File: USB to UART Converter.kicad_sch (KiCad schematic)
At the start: 19 parts, among them J1 USB_C_Receptacle_USB2.0_16P, J2 Conn_01x05_Pin, U1 CP2102N-Axx-xQFN28

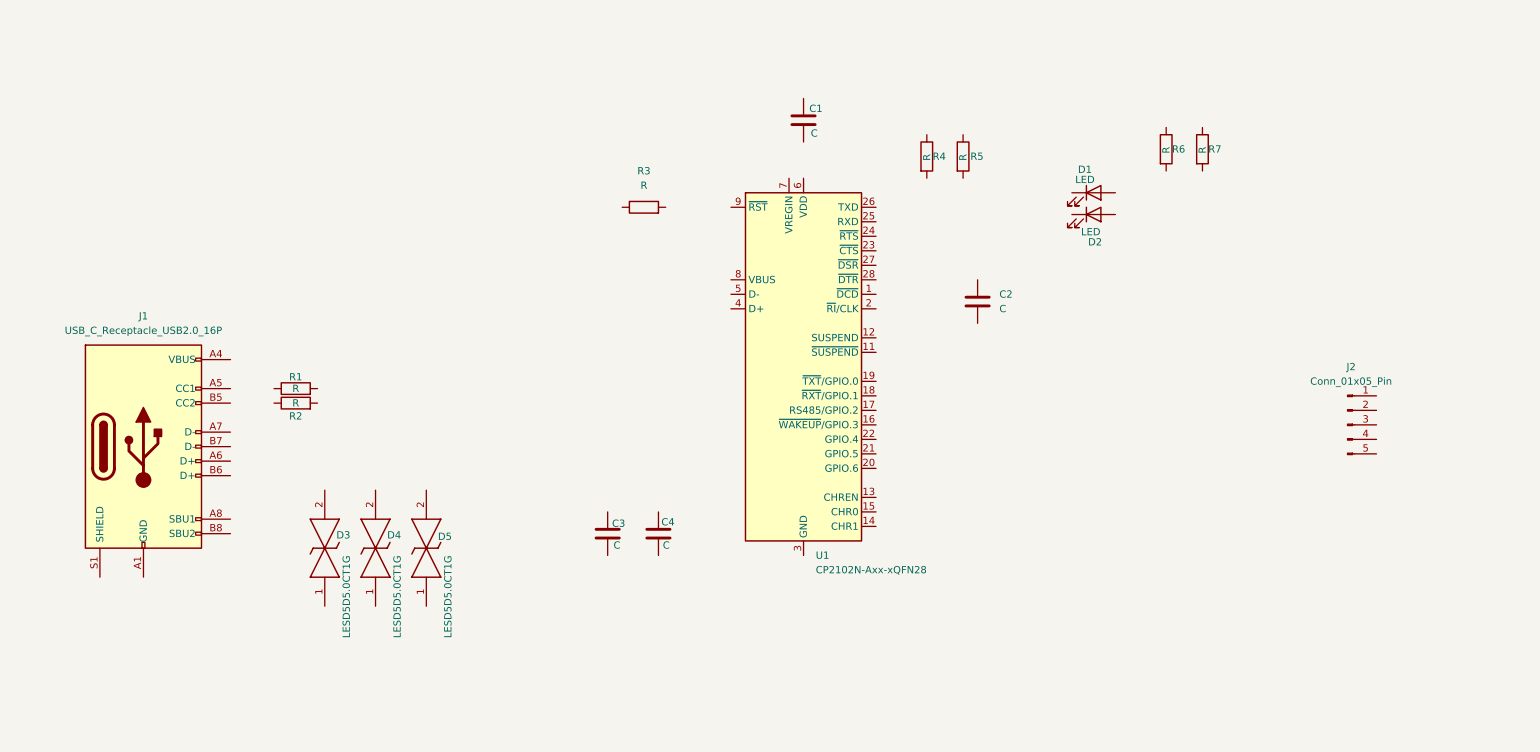
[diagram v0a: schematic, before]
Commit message: Connected with Wires in Schematic
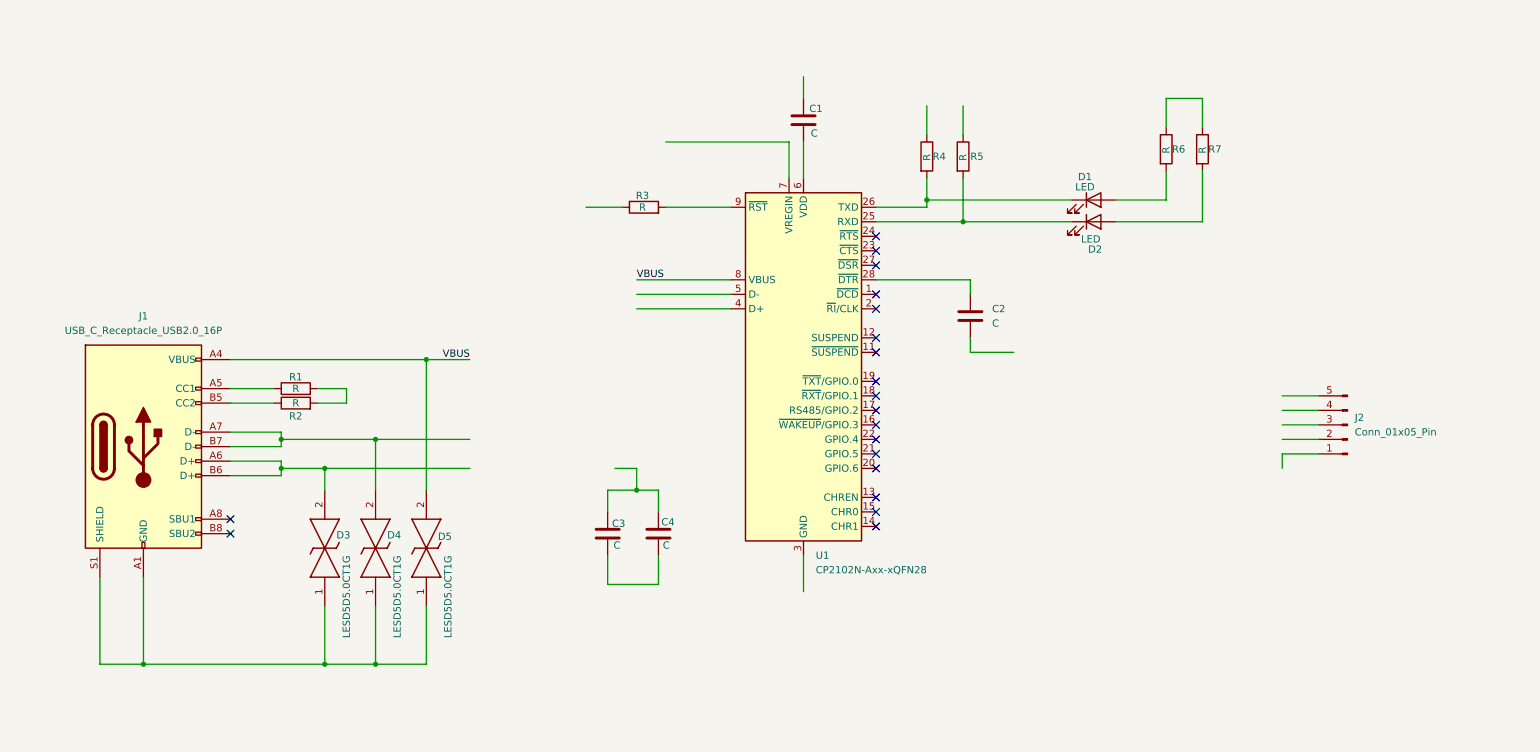
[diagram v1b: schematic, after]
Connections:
- net at D1.1 (K): now also R4.2, U1.26 (TXD)
- net at D1.2 (A): now also R6.2
- net at C1.2: now also U1.6 (VDD)
- net at R2.1: now also J1.B5 (CC2)
- net at R2.2: now also R1.2
- net at D2.1 (K): now also R5.2, U1.25 (RXD)
- net at D2.2 (A): now also R7.2
- net at U1.28 (~{DTR}): now also C2.1
- net VBUS: now reaches U1.8 (VBUS)
- net VBUS: now also D5.2, J1.A4 (VBUS), J1.A9 (VBUS), J1.B4 (VBUS), J1.B9 (VBUS)
- net at U1.9 (~{RST}): now also R3.2
- net at D4.1: now also D3.1, D5.1, J1.A1 (GND), J1.A12 (GND), J1.B1 (GND), J1.B12 (GND), J1.S1 (SHIELD)
- net at D4.2: now also J1.A7 (D-), J1.B7 (D-)
- net at R6.1: now also R7.1
- net at C4.1: now also C3.1
- net at C4.2: now also C3.2
- net at J1.A5 (CC1): now also R1.1
- net at J1.A6 (D+): now also D3.2, J1.B6 (D+)
- no-connect marks 0 -> 19
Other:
- moved on the sheet: C2, D1, D2, J2

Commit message: Added Net Labels
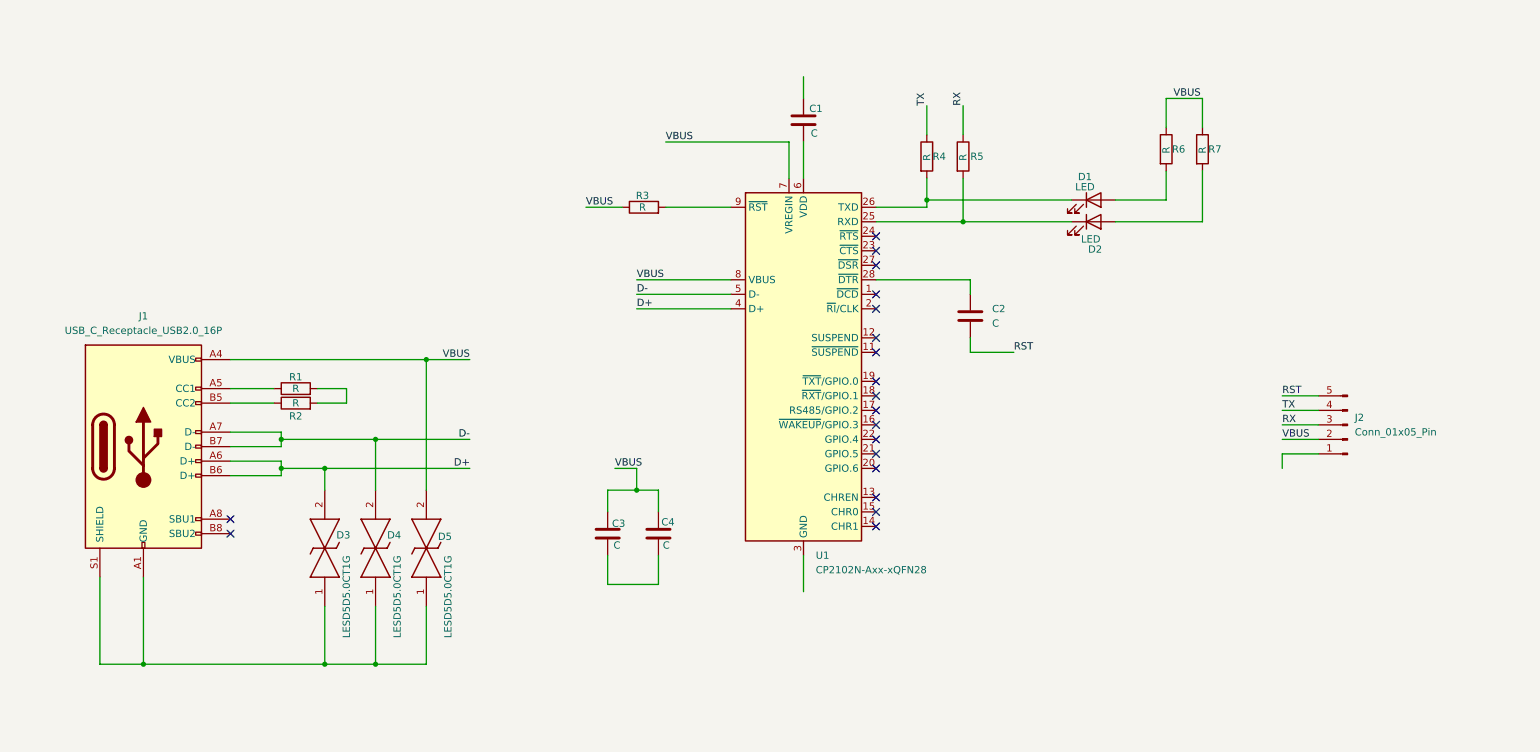
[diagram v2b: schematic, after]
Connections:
- net VBUS: now also C3.1, C4.1, J2.2 (Pin_2), R3.1, R6.1, R7.1, U1.7 (VREGIN)
- net D+: now reaches U1.4 (D+)
- net D+: now also D3.2, J1.A6 (D+), J1.B6 (D+)
- net D-: now reaches U1.5 (D-)
- net D-: now also D4.2, J1.A7 (D-), J1.B7 (D-)
- net RST: now reaches C2.2
- net RST: now also J2.5 (Pin_5)
- net RX: now reaches R5.1
- net RX: now also J2.3 (Pin_3)
- net TX: now reaches R4.1
- net TX: now also J2.4 (Pin_4)
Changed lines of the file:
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@@
+		)
+	)
+	(label "D+"
+		(at 128.27 71.12 0)
+		(effects
+			(font
+				(size 1.27 1.27)
+			)
+			(justify left bottom)
 		)
 	)
@@
 	)
 	(label "VBUS"
+		(at 133.35 41.91 0)
+		(effects
+			(font
+				(size 1.27 1.27)
+			)
+			(justify left bottom)
+		)
+	)
+	(label "D-"
+		(at 99.06 93.98 180)
+		(effects
+			(font
+				(size 1.27 1.27)
+			)
+			(justify right bottom)
+		)
+	)
+	(label "VBUS"
 		(at 128.27 66.04 0)
 		(effects
 			(font
+				(size 1.27 1.27)
+			)
+			(justify left bottom)
+		)
+	)
+	(label "VBUS"
+		(at 241.3 93.98 0)
+		(effects
+			(font
+				(size 1.27 1.27)
+			)
+			(justify left bottom)
+		)
+	)
+	(label "VBUS"
+		(at 124.46 99.06 0)
+		(effects
+			(font
+				(size 1.27 1.27)
+			)
+			(justify left bottom)
+		)
+	)
+	(label "TX"
+		(at 179.07 35.56 90)
+		(effects
+			(font
+				(size 1.27 1.27)
+			)
+			(justify left bottom)
+		)
+	)
+	(label "TX"
+		(at 241.3 88.9 0)
+		(effects
+			(font
+				(size 1.27 1.27)
+			)
+			(justify left bottom)
+		)
+	)
+	(label "D+"
+		(at 99.06 99.06 180)
+		(effects
+			(font
+				(size 1.27 1.27)
+			)
+			(justify right bottom)
+		)
+	)
+	(label "VBUS"
+		(at 222.25 34.29 0)
+		(effects
+			(font
+				(size 1.27 1.27)
+			)
+			(justify left bottom)
+		)
+	)
+	(label "RX"
+		(at 241.3 91.44 0)
+		(effects
+			(font
+				(size 1.27 1.27)
+			)
+			(justify left bottom)
+		)
+	)
+	(label "RST"
+		(at 241.3 86.36 0)
+		(effects
+			(font
+				(size 1.27 1.27)
+			)
+			(justify left bottom)
+		)
+	)
+	(label "VBUS"
+		(at 119.38 53.34 0)
+		(effects
+			(font
+				(size 1.27 1.27)
+			)
+			(justify left bottom)
+		)
+	)
+	(label "RST"
+		(at 194.31 78.74 0)
+		(effects
+			(font
+				(size 1.27 1.27)
+			)
+			(justify left bottom)
+		)
+	)
+	(label "RX"
+		(at 185.42 35.56 90)
+		(effects
+			(font
+				(size 1.27 1.27)
+			)
+			(justify left bottom)
+		)
+	)
+	(label "D-"
+		(at 128.27 68.58 0)
+		(effects
+			(font

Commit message: Placed GND and PWR flag
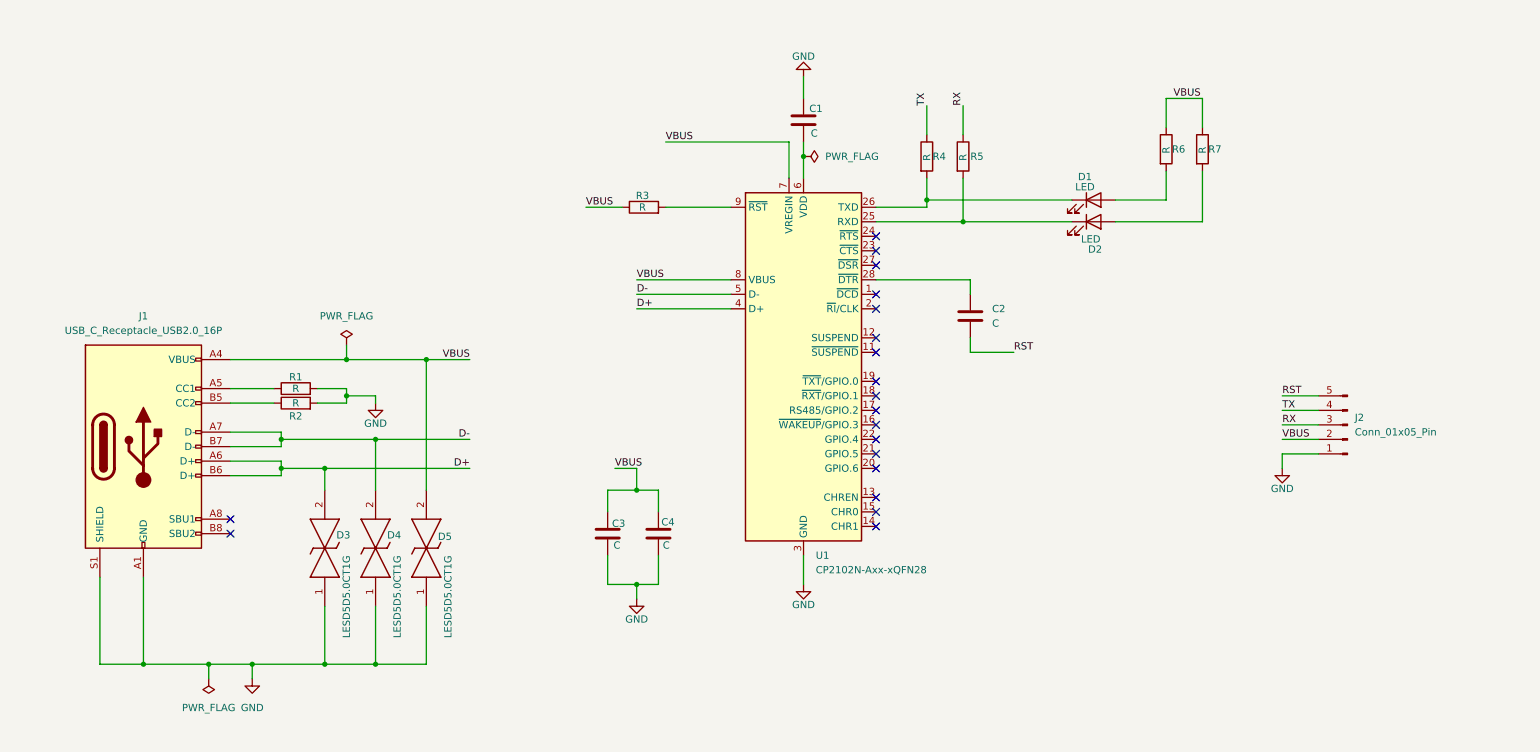
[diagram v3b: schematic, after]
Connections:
- net GND: now reaches C1.1
- net GND: now also C3.2, C4.2, D3.1, D4.1, D5.1, J1.A1 (GND), J1.A12 (GND), J1.B1 (GND), J1.B12 (GND), J1.S1 (SHIELD), J2.1 (Pin_1), R1.2, R2.2, U1.29 (GND), U1.3 (GND)

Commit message: Added Values to Components in Schematic
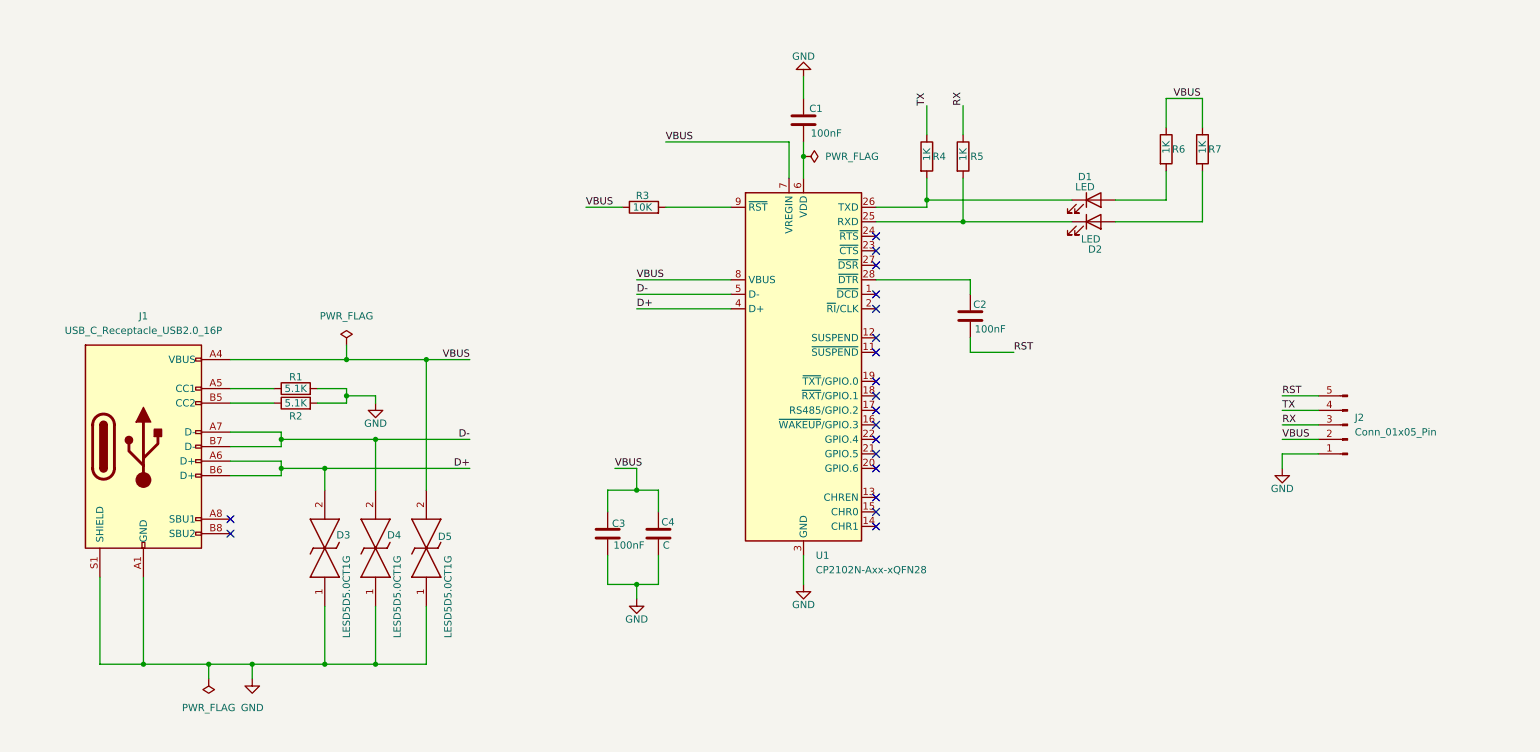
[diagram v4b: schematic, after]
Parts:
- C1, C2, C3: value C -> 100nF
- R1, R2: value R -> 5.1K
- R3: value R -> 10K
- R4, R5, R6, R7: value R -> 1K
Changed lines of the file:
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@@
 			)
 		)
-		(property "Value" "C"
+		(property "Value" "100nF"
 			(at 158.75 40.386 0)
 			(effects
@@
 			)
 		)
-		(property "Value" "R"
+		(property "Value" "5.1K"
 			(at 68.58 87.63 90)
 			(effects
@@
 		(on_board yes)
 		(dnp no)
-		(fields_autoplaced yes)
 		(property "Reference" "C2"
-			(at 190.5 71.1199 0)
+			(at 187.198 70.358 0)
 			(effects
 				(font
@@
 			)
 		)
-		(property "Value" "C"
-			(at 190.5 73.6599 0)
+		(property "Value" "100nF"
+			(at 187.452 74.676 0)
 			(effects
 				(font
@@
 			)
 		)
-		(property "Value" "R"
+		(property "Value" "1K"
 			(at 185.42 45.212 90)
 			(effects
@@
 			)
 		)
-		(property "Value" "R"
+		(property "Value" "1K"
 			(at 220.98 43.942 90)
 			(effects
@@
 			)
 		)
-		(property "Value" "R"
+		(property "Value" "1K"
 			(at 179.07 45.212 90)
 			(effects
@@
 			)
 		)
-		(property "Value" "R"
+		(property "Value" "10K"
 			(at 129.286 53.34 90)
 			(effects
@@
 			)
 		)
-		(property "Value" "R"
+		(property "Value" "1K"
 			(at 227.33 43.942 90)
 			(effects
@@
 			)
 		)
-		(property "Value" "C"
+		(property "Value" "100nF"
 			(at 124.206 112.522 0)
 			(effects
@@
 			)
 		)
-		(property "Value" "R"
+		(property "Value" "5.1K"
 			(at 68.58 85.09 90)
 			(effects

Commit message: Added Rectangles/Blocks
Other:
- note added: "CP2102"
- note added: "External Pins"
- note added: "USB Type-C"
- moved on the sheet: J2
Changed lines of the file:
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@@
 		(title "USB to UART Converter Project")
 	)
+	(rectangle
+		(start 237.49 19.05)
+		(end 280.035 146.05)
+		(stroke
+			(width 0)
+			(type default)
+		)
+		(fill
+			(type none)
+		)
+	)
+	(rectangle
+		(start 114.935 19.05)
+		(end 233.68 146.05)
+		(stroke
+			(width 0)
+			(type default)
+		)
+		(fill
+			(type none)
+		)
+	)
+	(rectangle
+		(start 20.32 19.05)
+		(end 109.22 146.685)
+		(stroke
+			(width 0)
+			(type default)
+		)
+		(fill
+			(type none)
+		)
+	)
+	(text "CP2102"
+		(exclude_from_sim no)
+		(at 130.556 24.638 0)
+		(effects
+			(font
+				(size 5.08 5.08)
+			)
+		)
+	)
+	(text "USB Type-C"
+		(exclude_from_sim no)
+		(at 45.466 26.67 0)
+		(effects
+			(font
+				(size 5.08 5.08)
+			)
+		)
+	)
+	(text "External Pins"
+		(exclude_from_sim no)
+		(at 258.826 23.622 0)
+		(effects
+			(font
+				(size 4.064 4.064)
+			)
+		)
+	)
 	(junction
 		(at 77.47 80.01)
@@
 	(wire
 		(pts
-			(xy 241.3 91.44) (xy 247.65 91.44)
+			(xy 248.92 90.17) (xy 255.27 90.17)
 		)
 		(stroke
@@
 	(wire
 		(pts
-			(xy 241.3 93.98) (xy 247.65 93.98)
+			(xy 248.92 92.71) (xy 255.27 92.71)
 		)
 		(stroke
@@
 	(wire
 		(pts
-			(xy 241.3 88.9) (xy 247.65 88.9)
+			(xy 248.92 87.63) (xy 255.27 87.63)
 		)
 		(stroke
@@
 	(wire
 		(pts
-			(xy 241.3 96.52) (xy 247.65 96.52)
+			(xy 248.92 95.25) (xy 255.27 95.25)
 		)
 		(stroke
@@
 	(wire
 		(pts
-			(xy 241.3 96.52) (xy 241.3 99.06)
+			(xy 248.92 95.25) (xy 248.92 97.79)
 		)
 		(stroke
@@
 	(wire
 		(pts
-			(xy 241.3 86.36) (xy 247.65 86.36)
+			(xy 248.92 85.09) (xy 255.27 85.09)
 		)
 		(stroke
@@
 	)
 	(label "VBUS"
-		(at 241.3 93.98 0)
+		(at 248.92 92.71 0)
 		(effects
 			(font
@@
 	)
 	(label "TX"
-		(at 241.3 88.9 0)
+		(at 248.92 87.63 0)
 		(effects
 			(font
@@
 	)
 	(label "RX"
-		(at 241.3 91.44 0)
+		(at 248.92 90.17 0)
 		(effects
 			(font
@@
 	)
 	(label "RST"
-		(at 241.3 86.36 0)
+		(at 248.92 85.09 0)
 		(effects
 			(font
@@
 	(symbol
 		(lib_id "power:GND")
-		(at 241.3 99.06 0)
+		(at 248.92 97.79 0)
 		(unit 1)
 		(exclude_from_sim no)
@@
 		(dnp no)
 		(property "Reference" "#PWR05"
-			(at 241.3 105.41 0)
+			(at 248.92 104.14 0)
 			(effects
 				(font
@@
 		)
 		(property "Value" "GND"
-			(at 241.3 102.616 0)
+			(at 248.92 101.346 0)
 			(effects
 				(font
@@
 		)
 		(property "Footprint" ""
-			(at 241.3 99.06 0)
+			(at 248.92 97.79 0)
 			(effects
 				(font
@@
 		)
 		(property "Datasheet" ""
-			(at 241.3 99.06 0)
+			(at 248.92 97.79 0)
 			(effects
 				(font
@@
 		)
 		(property "Description" "Power symbol creates a global label with name \"GND\" , ground"
-			(at 241.3 99.06 0)
+			(at 248.92 97.79 0)
 			(effects
 				(font
@@
 	(symbol
 		(lib_id "Connector:Conn_01x05_Pin")
-		(at 252.73 91.44 180)
+		(at 260.35 90.17 180)
 		(unit 1)
 		(exclude_from_sim no)
@@
 		(fields_autoplaced yes)
 		(property "Reference" "J2"
-			(at 254 90.1699 0)
+			(at 261.62 88.8999 0)
 			(effects
 				(font
@@
 		)
 		(property "Value" "Conn_01x05_Pin"
-			(at 254 92.7099 0)
+			(at 261.62 91.4399 0)
 			(effects
 				(font
@@
 		)
 		(property "Footprint" ""
-			(at 252.73 91.44 0)
+			(at 260.35 90.17 0)
 			(effects
 				(font
@@
 		)
 		(property "Datasheet" "~"
-			(at 252.73 91.44 0)
+			(at 260.35 90.17 0)
 			(effects
 				(font
@@
 		)
 		(property "Description" "Generic connector, single row, 01x05, script generated"
-			(at 252.73 91.44 0)
+			(at 260.35 90.17 0)
 			(effects
 				(font
